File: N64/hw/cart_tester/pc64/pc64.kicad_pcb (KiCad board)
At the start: 2 copper layers, 86.1 x 88.9 mm, 42 parts, among them CON1 HDR1X3, CON2 HDR1X3, CON3 HDR1X3, CON4 HDR1X3, J1 USB_C_Receptacle_USB2.0, J2 Conn_02x06_Odd_Even, SW1 BootButton, SW2 ResetButton, U1 RP2040, U2 N64-Cartridge, U3 W25Q128JVS, U4 NCP1117-3.3_SOT223, Y1 12MHz 10ppm

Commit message: Update dreamdumper board, sanity commit before redoing all routing
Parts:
- removed CON1, CON4: HDR1X3, db-thparts:HDR1X3
- removed J2: Conn_02x06_Odd_Even, Connector_PinHeader_2.54mm:PinHeader_2x06_P2.54mm_Vertical
- added J3: CART 12V IN, Connector_BarrelJack:BarrelJack_Horizontal, F.Cu at (72.6, 83.9)
- added kibuzzard-665BAD6D: G***, kibuzzard-665BAD6D, F.Cu at (136.4, 104.1)
- added kibuzzard-665BADED: G***, kibuzzard-665BADED, F.Cu at (87.4, 83.8)
- added kibuzzard-665BAE91: G***, kibuzzard-665BAE91, F.Cu at (82.7, 124.6)
- CON2, CON3: footprint db-thparts:HDR1X3 -> Connector_PinSocket_2.54mm:PinSocket_1x03_P2.54mm_Vertical
- moved CON3 70.1 mm to (68.2, 57.3)
- moved U2 62.4 mm to (83.1, 114.8), turned to 180 degrees
- moved CON2 57.0 mm to (68.2, 64.8), turned to 0 degrees
- moved R4 15.6 mm to (116.5, 45.8), turned to 180 degrees
- moved C6 14.3 mm to (110.8, 94.0), turned to -90 degrees
- moved C10 14.0 mm to (109.7, 94.0), turned to -90 degrees
- moved C14 14.0 mm to (101.9, 82.8), turned to 180 degrees
- moved C13 13.4 mm to (103.7, 88.2), turned to 180 degrees
- moved R3 13.3 mm to (98.5, 66.4), turned to 180 degrees
- moved R6 11.6 mm to (108.1, 57.6), turned to 180 degrees
- moved C3 10.7 mm to (129.9, 68.8), turned to 180 degrees
- moved C2 10.4 mm to (104.9, 66.3), turned to 180 degrees
- moved C4 9.55 mm to (105.3, 98.5), turned to 0 degrees
- moved R8 9.09 mm to (110.5, 80.9)
- moved R7 9.09 mm to (109.3, 81.0)
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- renumbered SW1 to Boot, U3 to Flash, G*** to Logo, SW2 to Reset
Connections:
- CON2 pad 1: /SWCLK -> /CART_VIDEO_SYNC
- CON2 pad 2: /SWDIO -> /CART_NMI
- CON2 pad 3: GND -> /CART_INT1
- U1 pad 35: /GPIO23 -> /N64_SI_DAT
- U1 pad 36: /UART1 TX -> /N64_SI_CLK
- U1 pad 37: /UART1 RX -> unconnected-(U1-GPIO25-Pad37)
- U1 pad 38: /GPIO26 -> unconnected-(U1-GPIO26_ADC0-Pad38)
- U1 pad 39: /GPIO27 -> unconnected-(U1-GPIO27_ADC1-Pad39)
- U1 pad 40: /GPIO28 -> unconnected-(U1-GPIO28_ADC2-Pad40)
- U1 pad 41: /GPIO29 -> unconnected-(U1-GPIO29_ADC3-Pad41)
- U2 pad 14: unconnected-(U2-Pad14) -> /CART_12V
- U2 pad 38: unconnected-(U2-Pad38) -> /CART_12V
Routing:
- net GND: track 307.1 -> 68.3 mm, vias 0 -> 20
- net +3V3: track 219.4 -> 40.1 mm, vias 4 -> 12
- net /N64_SI_DAT: track 0.00 -> 67.3 mm, vias 0 -> 1
- net /N64_SI_CLK: track 0.00 -> 60.5 mm, vias 0 -> 1
- net /AD15: track 73.3 -> 25.4 mm, vias 0 -> 2
- net /GPIO23: track 47.3 -> 0.00 mm
- net /AD14: track 69.1 -> 23.9 mm
- net /AD13: track 65.1 -> 22.2 mm, vias 0 -> 2
- net /GPIO26: track 33.9 -> 0.00 mm
- net /GPIO27: track 33.0 -> 0.00 mm
- net /GPIO28: track 32.1 -> 0.00 mm
- net /GPIO29: track 31.2 -> 0.00 mm
- net /UART1 RX: track 27.7 -> 0.00 mm
- net /ALEH: track 34.5 -> 61.9 mm, vias 1 -> 2
- net /UART1 TX: track 26.2 -> 0.00 mm
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- added copper zone on In1.Cu, net +3V3
- added copper zone on In2.Cu, net GND
- added copper zone on In1.Cu, net VBUS
- removed copper zone on F.Cu, net GND
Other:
- copper layers 2 -> 4
- board text added: "NMI"
- board text added: "VSync"
- board text added: "dreamcraftindustries.com 06-01-2024"
- board text removed: "3v3"
- board text removed: "CART"
- board text removed: "CIC"
- board text removed: "CLK"
- board text removed: "Cart Tester 64 prototype v1 Kaili Hill 12-16-2022"
- board text removed: "DIO"
- board text removed: "GPIO23"
- board text removed: "GPIO26"
- board text removed: "GPIO27"
- board text removed: "GPIO28"
- board text removed: "GPIO29"
- board text removed: "RX"
- board text removed: "SWCLK"
- board text removed: "SWD Debugger"
- board text removed: "SWDIO"
- board text removed: "TX"
- board text removed: "UART1"

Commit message: Another pass at the dreamdumper board
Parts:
- removed Boot: BootButton, Button_Switch_SMD:SW_SPST_FSMSM
- removed C1: 10u, Capacitor_SMD:C_0603_1608Metric
- removed C12, C2: 100n, Capacitor_SMD:C_0402_1005Metric
- removed Flash: W25Q128JVS, Package_SO:SOIC-8_5.23x5.23mm_P1.27mm
- removed R5: 5k1, Resistor_SMD:R_0402_1005Metric
- removed R6: 10k, Resistor_SMD:R_0402_1005Metric
- removed R7, R8: 22R, Resistor_SMD:R_0402_1005Metric
- removed Reset: ResetButton, Button_Switch_SMD:SW_SPST_FSMSM
- removed U1: RP2040, Package_DFN_QFN:QFN-56-1EP_7x7mm_P0.4mm_EP3.2x3.2mm
- added C1001: 1uF, Capacitor_SMD:C_0402_1005Metric, F.Cu at (109.7, 46.7)
- added C1002: 1uF, Capacitor_SMD:C_0402_1005Metric, F.Cu at (109.7, 54.9)
- added C16: 100nF, Capacitor_SMD:C_0402_1005Metric, F.Cu at (108.4, 92.8)
- added F1: 1.1A, Fuse:Fuse_1206_3216Metric, F.Cu at (122.5, 53.8)
- added R1001: 1K, Resistor_SMD:R_0402_1005Metric, F.Cu at (107.0, 93.2)
- added RP_SW1: SW_Push, Button_Switch_SMD:SW_SPST_TL3342, F.Cu at (132.0, 76.2)
- added RP_SW2: SW_Push, Button_Switch_SMD:SW_SPST_TL3342, F.Cu at (131.9, 86.5)
- added U1001: SRV05-4, Package_TO_SOT_SMD:SOT-23-6, F.Cu at (122.5, 50.9)
- added U1002: AMS1117-3.3, Package_TO_SOT_SMD:SOT-223, F.Cu at (106.2, 50.8)
- added U3: W25Q128JVS, Package_SO:SOIC-8_5.23x5.23mm_P1.27mm, F.Cu at (102.7, 78.5)
- C10, C11, C13, C14, C15, C6: value 100n -> 100nF
- C3: value 10u -> 30pF; footprint Capacitor_SMD:C_0603_1608Metric -> Capacitor_SMD:C_0402_1005Metric
- C4: value 12p -> 30pF
- C5: value 12p -> 100nF
- C7: value 100n -> 1uF
- C8: value 1u -> 1uF
- C9: value 1u -> 100nF
- J1: footprint Connector_USB:USB_C_Receptacle_XKB_U262-16XN-4BVC11 -> JBroekCustom:HRO-TYPE-C-31-M-12_LCSC
- J2: renamed from J3; value CART 12V IN -> CART 12V
- R1: value 1K -> 5k1
- R2: value 100k -> 5k1
- R3: value 10K -> 27
- R4: value 5k1 -> 27
- U4: value NCP1117-3.3_SOT223 -> RP2040; footprint Package_TO_SOT_SMD:SOT-223-3_TabPin2 -> JBroekCustom:RP2040-QFN-56
- Y1: value 12MHz 10ppm -> Crystal_GND24; footprint Crystal:Crystal_SMD_2520-4Pin_2.5x2.0mm -> Crystal:Crystal_SMD_3225-4Pin_3.2x2.5mm
- moved J2 36.4 mm to (94.2, 54.6), turned to -90 degrees
- moved C3 35.9 mm to (102.7, 92.3), turned to -90 degrees
- moved U4 35.6 mm to (106.4, 87.2), turned to 0 degrees
- moved R4 35.5 mm to (108.1, 80.4), turned to 90 degrees
- moved R1 31.9 mm to (127.5, 45.7)
- moved R3 16.4 mm to (107.1, 80.4), turned to 90 degrees
- moved C5 15.7 mm to (106.1, 82.2), turned to -90 degrees
- moved C10 10.0 mm to (111.0, 84.0)
- moved C11 9.21 mm to (111.5, 88.2), turned to 180 degrees
- moved Logo 8.33 mm to (124.0, 118.4)
- moved C15 8.03 mm to (107.0, 82.2), turned to -90 degrees
- moved kibuzzard-665BAD6D 7.60 mm to (131.7, 110.1)
- moved kibuzzard-665BADED 6.56 mm to (93.5, 86.2)
- moved C4 4.48 mm to (107.5, 94.6)
- moved C6 3.16 mm to (108.4, 91.9), turned to 180 degrees
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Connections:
- C10 pad 1: +3V3 -> GND
- C10 pad 2: GND -> 3.3V
- C11 pad 1: +3V3 -> GND
- C11 pad 2: GND -> 3.3V
- C13 pad 1: +3V3 -> GND
- C13 pad 2: GND -> 3.3V
- C14 pad 1: +3V3 -> GND
- C14 pad 2: GND -> 3.3V
- C15 pad 1: +3V3 -> GND
- C15 pad 2: GND -> 3.3V
- C3 pad 1: +3V3 -> Net-(U4-XIN)
- C4 pad 1: GND -> Net-(C4-Pad1)
- C4 pad 2: /MCU1_XIN -> GND
- C5 pad 2: /MCU1_XOUT -> Net-(U4-VREG_VOUT)
- C6 pad 1: Net-(U1-VREG_VOUT) -> GND
- C6 pad 2: GND -> Net-(U4-VREG_VOUT)
- C7 pad 1: Net-(U1-VREG_VOUT) -> GND
- C7 pad 2: GND -> Net-(U4-VREG_VOUT)
- C8 pad 1: Net-(U1-VREG_VOUT) -> GND
- C8 pad 2: GND -> 3.3V
- C9 pad 1: +3V3 -> GND
- C9 pad 2: GND -> 3.3V
- J1 pad A4: VBUS -> Net-(F1-Pad2)
- J1 pad A6: /USB_D+ -> USB_D+
- J1 pad A7: /USB_D- -> USB_D-
- J1 pad A9: VBUS -> Net-(F1-Pad2)
- J1 pad B4: VBUS -> Net-(F1-Pad2)
- J1 pad B6: /USB_D+ -> USB_D+
- J1 pad B7: /USB_D- -> USB_D-
- J1 pad B9: VBUS -> Net-(F1-Pad2)
- J1 pad S1: Net-(J1-SHIELD) -> GND
- R1 pad 1: /~{SSI_CS} -> GND
- R1 pad 2: Net-(R1-Pad2) -> Net-(J1-CC1)
- R2 pad 2: Net-(J1-SHIELD) -> Net-(J1-CC2)
- R3 pad 1: +3V3 -> Net-(U4-USB_DP)
- R3 pad 2: /~{SSI_CS} -> USB_D+
- R4 pad 1: Net-(J1-CC1) -> Net-(U4-USB_DM)
- R4 pad 2: GND -> USB_D-
- U2 pad 17: +3V3 -> 3.3V
- U2 pad 34: +3V3 -> 3.3V
- U2 pad 42: +3V3 -> 3.3V
- U2 pad 9: +3V3 -> 3.3V
- U4 pad 1: GND -> 3.3V
- U4 pad 2: +3V3 -> /AD0
- U4 pad 3: VBUS -> /AD1
- U4 pad 4: (no net) -> /AD2
- Y1 pad 1: /MCU1_XOUT -> Net-(C4-Pad1)
- Y1 pad 3: /MCU1_XIN -> Net-(U4-XIN)
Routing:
- net /RUN: track 63.0 -> 0.00 mm, vias 2 -> 0
- net 3.3V: track 0.00 -> 47.5 mm, vias 0 -> 12
- net QSPI_CSn_Pull: track 0.00 -> 45.2 mm, vias 0 -> 2
- net /CART_12V: track 25.4 -> 66.9 mm
- net USB_D+: track 0.00 -> 41.4 mm
- net USB_D-: track 0.00 -> 40.9 mm
- net /USB_D+: track 40.9 -> 0.00 mm
- net /USB_D-: track 40.7 -> 0.00 mm
- net +3V3: track 40.1 -> 0.00 mm, vias 12 -> 0
- net RUN_PULL: track 0.00 -> 32.4 mm
- net /~{SSI_CS}: track 31.4 -> 0.00 mm
- net VBUS: track 29.7 -> 0.00 mm, vias 4 -> 0
- net Net-(U1-VREG_VOUT): track 21.8 -> 0.00 mm
- net /SSI_SD1: track 19.2 -> 0.00 mm
- net /AD4: track 11.8 -> 30.9 mm, vias 1 -> 2
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- added copper zone on F.Cu, net 3.3V
- added copper zone on In1.Cu, net 3.3V
- added copper zone on F.Cu, net 5V
- added copper zone on In1.Cu, net 5V
- added copper zone on F.Cu, net GND
- removed copper zone on In1.Cu, net +3V3
- removed copper zone on In1.Cu, net VBUS
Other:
- board text added: "12v"
- board text added: "3.3v"
- board text added: "AD0"
- board text added: "AD1"
- board text added: "AD10"
- board text added: "AD11"
- board text added: "AD12"
- board text added: "AD13"
- board text added: "AD14"
- board text added: "AD15"
- board text added: "AD2"
- board text added: "AD3"
- board text added: "AD4"
- board text added: "AD5"
- board text added: "AD6"
- board text added: "AD7"
- board text added: "AD8"
- board text added: "AD9"
- board text added: "ALEH"
- board text added: "ALEL"
- board text added: "CIC CLK"
- board text added: "CIC DIO"
- board text added: "Cold Reset"
- board text added: "LAUDIO"
- board text added: "RAUDIO"
- board text added: "READ"
- board text added: "SI CLK"
- board text added: "SI DAT"
- board text added: "VSYNC"
- board text added: "WRITE"

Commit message: Updated the dreamdumper64 stand alone board. This was submitted for test samples.
Rewrote a bunch of dreamdrivecast code, it isn't tested but should be a lot faster if it works.
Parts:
- CART 12V: renamed from J2; footprint Connector_BarrelJack:BarrelJack_Horizontal -> Connector_BarrelJack:BarrelJack_CUI_PJ-036AH-SMT_Horizontal
- moved U1002 27.5 mm to (132.3, 59.6), turned to -90 degrees
- moved C1002 26.8 mm to (136.4, 56.1), turned to 90 degrees
- moved C1001 23.9 mm to (132.5, 54.0), turned to 0 degrees
- moved CART 12V 12.8 mm to (106.6, 51.3), turned to 180 degrees
- moved F1 3.25 mm to (125.7, 53.9)
- moved J1 3.25 mm to (125.7, 45.8)
- moved R1 3.25 mm to (130.8, 45.8)
- moved R2 3.25 mm to (120.7, 45.8)
- moved U1001 3.25 mm to (125.7, 51.1)
- moved CON2 2.30 mm to (65.9, 65.0)
- moved CON3 2.29 mm to (65.9, 57.5)
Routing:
- net /CART_12V: track 66.9 -> 85.4 mm, vias 0 -> 4
- net /AD4: track 30.9 -> 47.0 mm, vias 2 -> 0
- net /AD13: track 35.7 -> 50.1 mm, vias 2 -> 0
- net /AD12: track 29.4 -> 40.9 mm, vias 2 -> 0
- net USB_D-: track 40.9 -> 50.6 mm
- net USB_D+: track 41.4 -> 50.7 mm
- net /AD6: track 30.5 -> 39.5 mm, vias 2 -> 0
- net /READ: track 55.3 -> 49.3 mm, vias 4 -> 2
- net /AD7: track 34.9 -> 40.3 mm, vias 1 -> 0
- net /AD5: track 26.0 -> 31.2 mm
- net 3.3V: track 47.5 -> 43.0 mm, vias 12 -> 7
- net /AD14: track 38.0 -> 34.0 mm, vias 2 -> 1
- net /COLD_RESET: track 58.8 -> 55.9 mm, vias 2 -> 1
- net /N64_SI_DAT: track 61.7 -> 58.8 mm, vias 2 -> 1
- net /AD9: track 28.8 -> 26.0 mm, vias 2 -> 1
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- added copper zone on B.Cu, net /CART_12V
- added copper zone on F.Cu, net /CART_12V
- removed copper zone on In1.Cu, net 5V

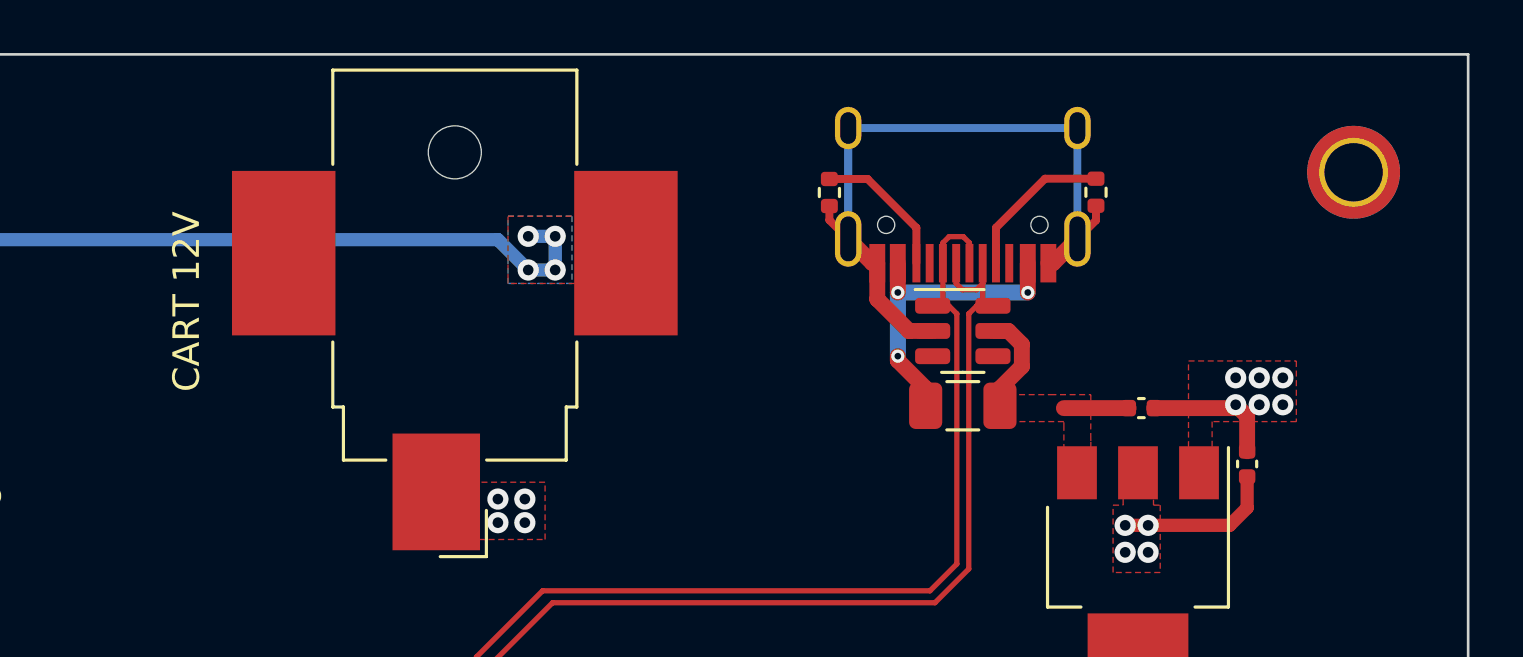
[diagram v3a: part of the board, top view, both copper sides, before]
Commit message: MIXED COMMIT: Dreamcast related: Data looks like it's flowing correctly! Dreamdrive: Modifed ctr0.s file has been included so others can drop into their pico-sdk folder. Dumper files have been updated with new design.
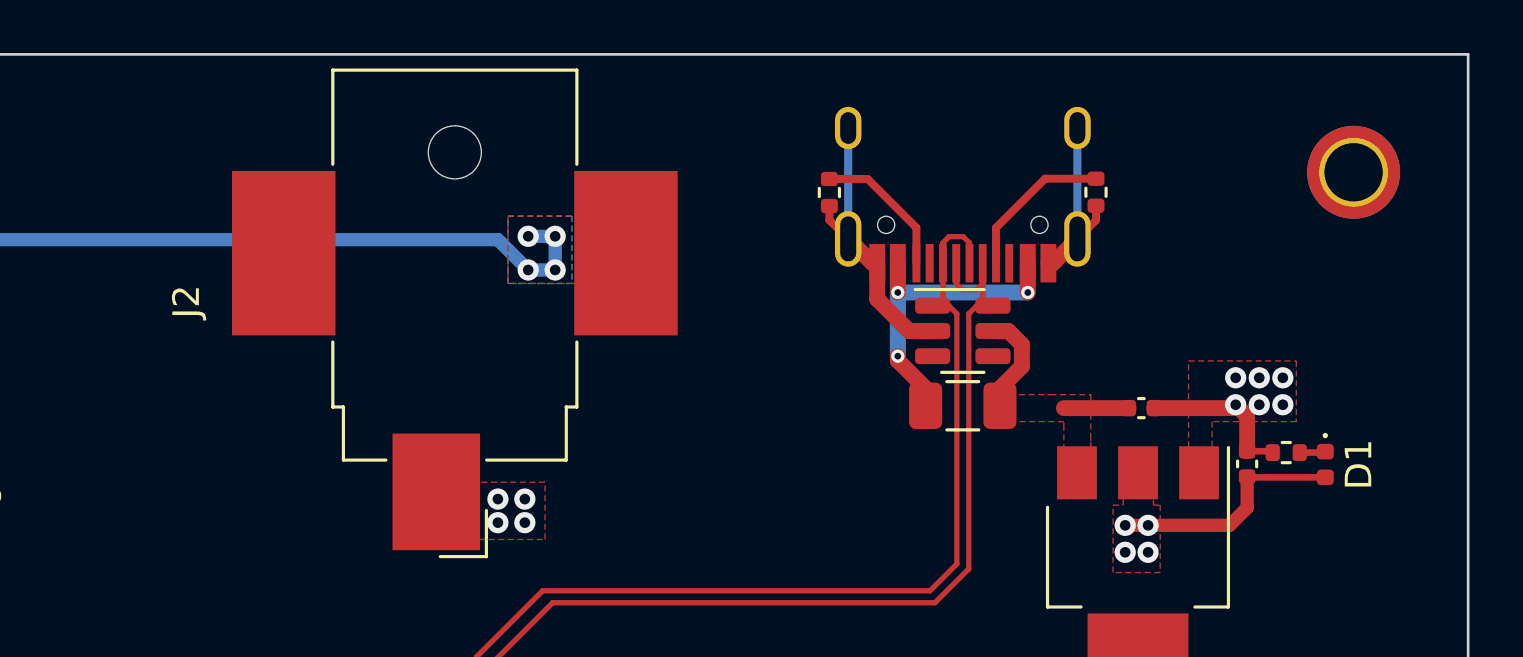
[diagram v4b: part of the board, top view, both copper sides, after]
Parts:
- added D1: PowerLED, LED_SMD:LED_0402_1005Metric, F.Cu at (139.4, 56.1)
- added R5: 35, Resistor_SMD:R_0402_1005Metric, F.Cu at (137.9, 55.7)
- J2: renamed from CART 12V; value CART 12V -> Barrel_Jack
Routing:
- net GND: track 74.1 -> 66.5 mm
- net 3.3V: track 43.0 -> 45.9 mm
- net Net-(D1-K): track 0.00 -> 0.98 mm
